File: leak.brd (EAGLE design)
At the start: 160 x 100 mm, 20 parts, among them IC1 74HC595D, IC2 74HC595D

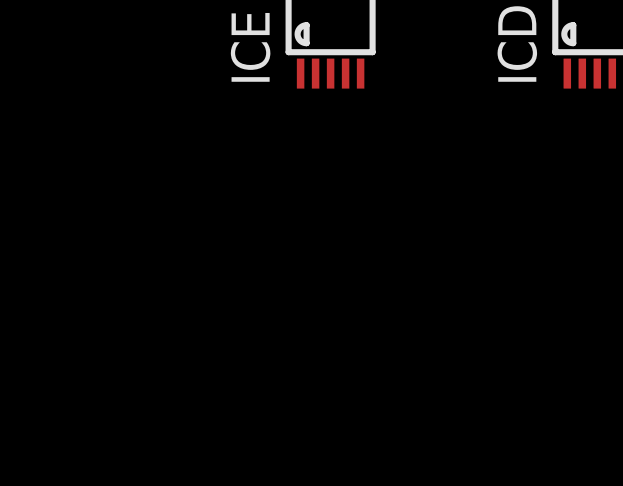
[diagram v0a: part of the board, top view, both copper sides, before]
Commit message: added link to a viewer and op amp
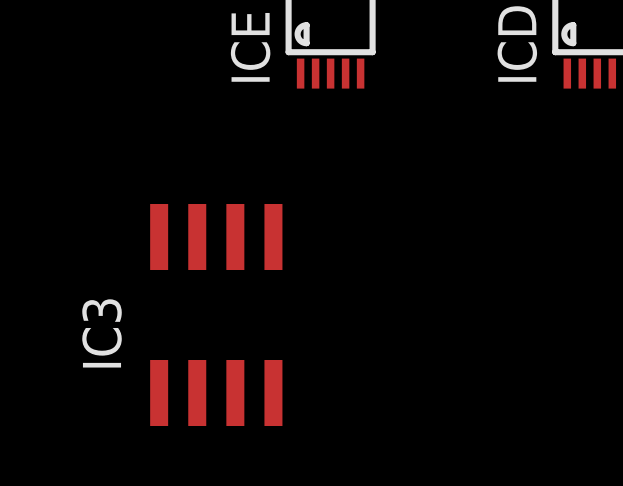
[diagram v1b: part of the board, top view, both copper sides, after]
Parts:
- added IC3: ADA4692-2R, analog-devices:SO8
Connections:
- new net V+: IC3.8
- new net V-: IC3.4
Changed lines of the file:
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@@
 <attribute name="VALUE" x="-30.988" y="16.51" size="1.27" layer="27" ratio="10" rot="R90"/>
+</element>
+<element name="IC3" library="analog-devices" library_urn="urn:adsk.eagle:library:102" package="SO8" package3d_urn="urn:adsk.eagle:package:30987/2" value="ADA4692-2R" x="-46.99" y="-6.35" smashed="yes">
+<attribute name="MF" value="" x="-46.99" y="-6.35" size="1.778" layer="27" display="off"/>
+<attribute name="MPN" value="ADA4692-2ARZ" x="-46.99" y="-6.35" size="1.778" layer="27" display="off"/>
+<attribute name="NAME" x="-50.165" y="-8.255" size="1.27" layer="25" rot="R90"/>
+<attribute name="OC_FARNELL" value="1760810" x="-46.99" y="-6.35" size="1.778" layer="27" display="off"/>
+<attribute name="OC_NEWARK" value="05R6523" x="-46.99" y="-6.35" size="1.778" layer="27" display="off"/>
+<attribute name="POPULARITY" value="0" x="-46.99" y="-6.35" size="1.778" layer="27" display="off"/>
+<attribute name="VALUE" x="-42.545" y="-8.255" size="1.27" layer="27" rot="R90"/>
 </element>
 </elements>
@@
 <wire x1="-27.305" y1="34.8234" x2="13.335" y2="23.3934" width="0" layer="19" extent="1-1"/>
 </signal>
+<signal name="V+">
+<contactref element="IC3" pad="8"/>
+</signal>
+<signal name="V-">
+<contactref element="IC3" pad="4"/>
+</signal>
 </signals>

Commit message: finished schematic
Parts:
- added C10: 10nF, rcl:C0603
- added C11, C12: 2uF, rcl:C0603
- added C13: 2uF, rcl:C0805K
- added C8, C9: 1uF, rcl:C0603
- added R1: 1M, rcl:R0805
- added R2: 10K, rcl:R0805
- added R3: 4.7K, rcl:R0805
- added U$1: TLV703, titled:SOT95P280X145-5N
- added U1: TPS72301DBVRSOT-23-5, titled:SOT95P280X145-5N
- moved IC3 88.4 mm to (36.8, 21.6)
- moved JP1 65.2 mm to (11.4, 6.35)
- moved IC1 55.9 mm to (25.4, 34.3)
- moved ICA 50.0 mm to (10.2, 41.9)
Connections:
- removed net V+: IC3.8
- removed net V-: IC3.4
- new net N$1: C10.2, U1.4
- new net N$2: IC3.1, IC3.5, R2.2, R3.2
- new net N$4: IC3.7
- new net N$6: IC3.2, R1.2, R2.1
- net +2V5: now also C12.2, IC3.8, U$1.5
- net +5V: now also C11.2, U$1.1, U$1.3
- net -2V5: now also C8.2, IC3.4, U1.5
- net -5V: now also C9.2, U1.2, U1.3
- net GND: now also C10.1, C11.1, C12.1, C13.2, C8.1, C9.1, R1.1, U$1.2, U1.1
- net LVLW: now also IC3.6
- net W: now also C13.1, IC3.3, R3.1
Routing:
- added copper zone on layer 1, net GND
- added copper zone on layer 16, net GND

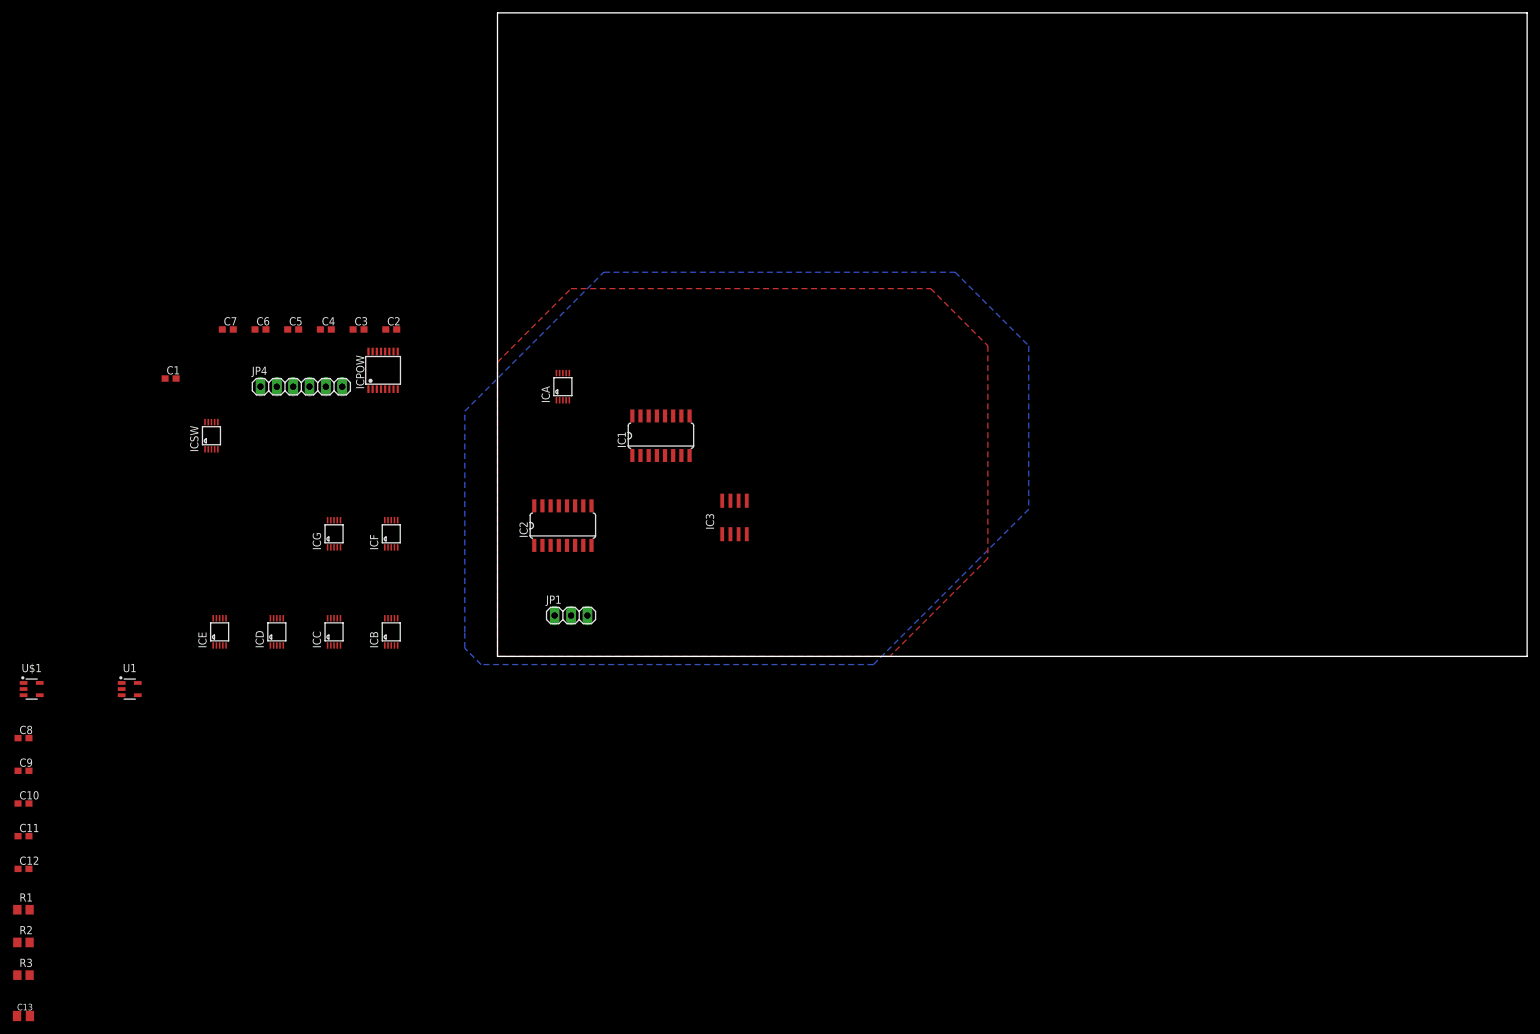
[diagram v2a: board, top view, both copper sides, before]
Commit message: started pcb layout
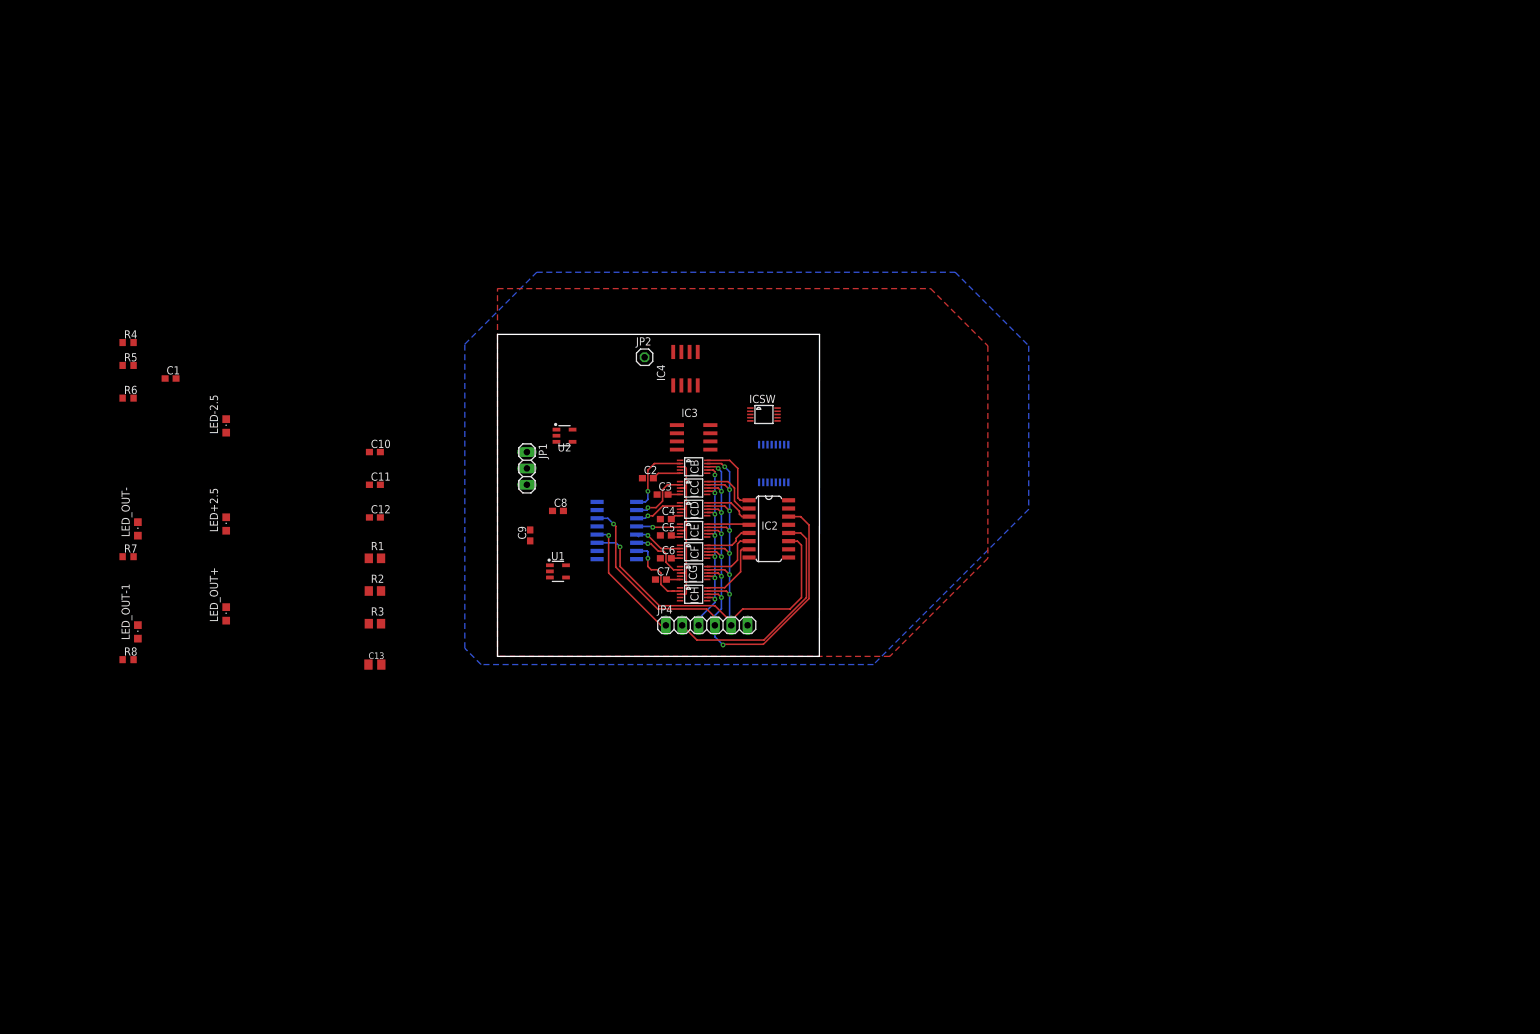
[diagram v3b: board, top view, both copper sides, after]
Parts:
- removed ICA: AD5270MSOP10, untitled:MSOP10
- removed U$1: TLV703, titled:SOT95P280X145-5N
- added IC4: ADA4692-2R, analog-devices:SO8
- added ICH: AD5270MSOP10, untitled:MSOP10
- added JP2: (no value), pinhead:1X01
- added LED+2.5, LED-2.5, LED_OUT+, LED_OUT-, LED_OUT-1: (no value), led:CHIPLED_0805
- added R4, R5, R6, R7, R8: 200, rcl:R0603
- added U2: TLV703, titled:SOT95P280X145-5N
- moved C8 90.3 mm to (9.40, 22.6)
- moved C9 86.8 mm to (5.08, 18.8), turned to 90 degrees
- moved ICSW 85.9 mm to (41.4, 37.6), turned to 270 degrees
- moved C7 77.7 mm to (25.4, 11.9)
- moved C10 77.2 mm to (-19.1, 31.8)
- moved C11 77.2 mm to (-19.1, 26.7)
- moved C12 77.2 mm to (-19.1, 21.6)
- moved C13 77.2 mm to (-19.1, -1.27)
- moved R1 77.2 mm to (-19.1, 15.2)
- moved R2 77.2 mm to (-19.1, 10.2)
- moved R3 77.2 mm to (-19.1, 5.08)
- moved ICE 75.3 mm to (30.5, 19.6), turned to 270 degrees
- moved JP4 73.1 mm to (32.5, 4.83)
- moved C6 72.3 mm to (26.2, 15.2)
- moved U1 69.0 mm to (9.40, 13.2)
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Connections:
- removed net RESET: IC1.10, IC2.10
- new net N$10: LED_OUT-.A, R7.2
- new net N$12: LED_OUT-1.C, R8.2
- new net N$7: LED+2.5.C, R5.2
- new net N$9: LED_OUT+.C, R6.2
- new net OUT: IC3.7, IC4.1, IC4.2, IC4.3, JP2.1, LED_OUT+.A, LED_OUT-.C, LED_OUT-1.A
- net +2V5: now also IC1.10, IC2.10, IC4.8, ICH.1, LED+2.5.A, U2.5; no longer ICA.1, U$1.5
- net +5V: now also U2.1, U2.3; no longer U$1.1, U$1.3
- net -2V5: now also ICH.4, LED-2.5.C; no longer ICA.4
- net AQA: no longer ICA.2
- net AQH: now also ICH.2
- net CSA: now also ICPOW.14; no longer ICA.10
- net CSH: now also ICH.10; no longer ICPOW.14
- net GND: now also IC4.4, ICH.6, R4.1, R5.1, R6.1, R7.1, R8.1, U2.2; no longer ICA.6, U$1.2
- net MISO: now also ICH.7, JP4.3; no longer ICA.7, JP4.4
- net MOSI: now also ICH.8, JP4.4; no longer ICA.8, JP4.3
- net N$4: now also LED-2.5.A, R4.2; no longer IC3.7
- net N$5: now also ICH.5; no longer ICA.5
- net SCLK: now also ICH.9; no longer ICA.9
- net W: now also ICH.3; no longer ICA.3
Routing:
- net MOSI: track 0.00 -> 106.2 mm, vias 0 -> 9
- net SCLK: track 0.00 -> 102.4 mm, vias 0 -> 8
- net CS_CS: track 0.00 -> 35.3 mm
- net MISO: track 0.00 -> 34.0 mm, vias 0 -> 7
- net W: track 0.00 -> 25.8 mm
- net CS_IN: track 0.00 -> 20.0 mm, vias 0 -> 1
- net AQB: track 0.00 -> 11.9 mm, vias 0 -> 1
- net CSB: track 0.00 -> 11.7 mm
- net AQH: track 0.00 -> 11.7 mm, vias 0 -> 1
- net CSH: track 0.00 -> 10.9 mm
- net CSG: track 0.00 -> 9.62 mm
- net AQC: track 0.00 -> 9.57 mm, vias 0 -> 1
- net CSC: track 0.00 -> 9.42 mm
- net AQG: track 0.00 -> 9.28 mm, vias 0 -> 1
- net AQF: track 0.00 -> 8.12 mm, vias 0 -> 1
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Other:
- board size 160 x 100 mm -> 50 x 50 mm

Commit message: v1 finished
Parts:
- removed LED_OUT+, LED_OUT-, LED_OUT-1: (no value), led:CHIPLED_0805
- added BIPOUT+, BIPOUT-, LEDOUT: (no value), led:CHIPLED_0805
- moved R8 85.5 mm to (16.0, 43.3)
- moved R4 83.5 mm to (12.8, 3.68), turned to 90 degrees
- moved C1 76.8 mm to (17.9, 8.89)
- moved R7 68.4 mm to (5.71, 41.8)
- moved R5 65.2 mm to (6.22, 31.0)
- moved R6 63.1 mm to (5.71, 39.8)
- moved LED-2.5 60.0 mm to (9.02, 4.57), turned to 90 degrees
- moved LED+2.5 54.2 mm to (11.0, 31.0), turned to 90 degrees
- moved C13 47.9 mm to (14.1, 33.3), turned to 270 degrees
- moved R2 44.2 mm to (16.1, 37.0), turned to 90 degrees
- moved R3 43.8 mm to (11.8, 36.2), turned to 90 degrees
- moved R1 39.8 mm to (14.1, 37.2), turned to 270 degrees
- moved C10 35.2 mm to (5.33, 6.35)
- moved C12 31.8 mm to (12.1, 28.2), turned to 90 degrees
- moved C11 23.6 mm to (4.45, 28.3), turned to 90 degrees
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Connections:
- removed net AQA: IC1.15
- new net OUT_BIP: BIPOUT+.A, BIPOUT-.C, IC3.7, IC4.3
- net +2V5: now also ICSW.10
- net +5V: no longer ICSW.10
- net -2V5: now also ICSW.5
- net -5V: no longer ICSW.5
- net N$10: now also BIPOUT-.A; no longer LED_OUT-.A
- net N$12: now also LEDOUT.C; no longer LED_OUT-1.C
- net N$9: now also BIPOUT+.C; no longer LED_OUT+.C
- net OUT: now also LEDOUT.A; no longer IC3.7, IC4.3, LED_OUT+.A, LED_OUT-.C, LED_OUT-1.A
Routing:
- net +2V5: track 0.00 -> 145.7 mm, vias 0 -> 12
- net -2V5: track 0.00 -> 108.1 mm, vias 0 -> 13
- net OUT_BIP: track 0.00 -> 18.1 mm
- net N$2: track 0.00 -> 16.0 mm
- net W: track 25.8 -> 41.2 mm
- net CSA: track 0.00 -> 14.9 mm, vias 0 -> 1
- net +5V: track 0.00 -> 13.8 mm
- net LVLW: track 0.00 -> 12.6 mm, vias 0 -> 1
- net OUT: track 0.00 -> 12.1 mm
- net O1: track 0.00 -> 10.8 mm
- net -5V: track 0.00 -> 10.6 mm
- net O2: track 0.00 -> 10.3 mm
- net LVLA: track 0.00 -> 8.25 mm
- net MISO: track 34.0 -> 41.6 mm
- net MOSI: track 106.2 -> 112.2 mm
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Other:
- board size 50 x 50 mm -> 40.6 x 48.3 mm
